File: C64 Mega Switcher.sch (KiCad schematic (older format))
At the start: 11 parts, among them J1 Port 2, J2 Port 1, J3 sega_joypad

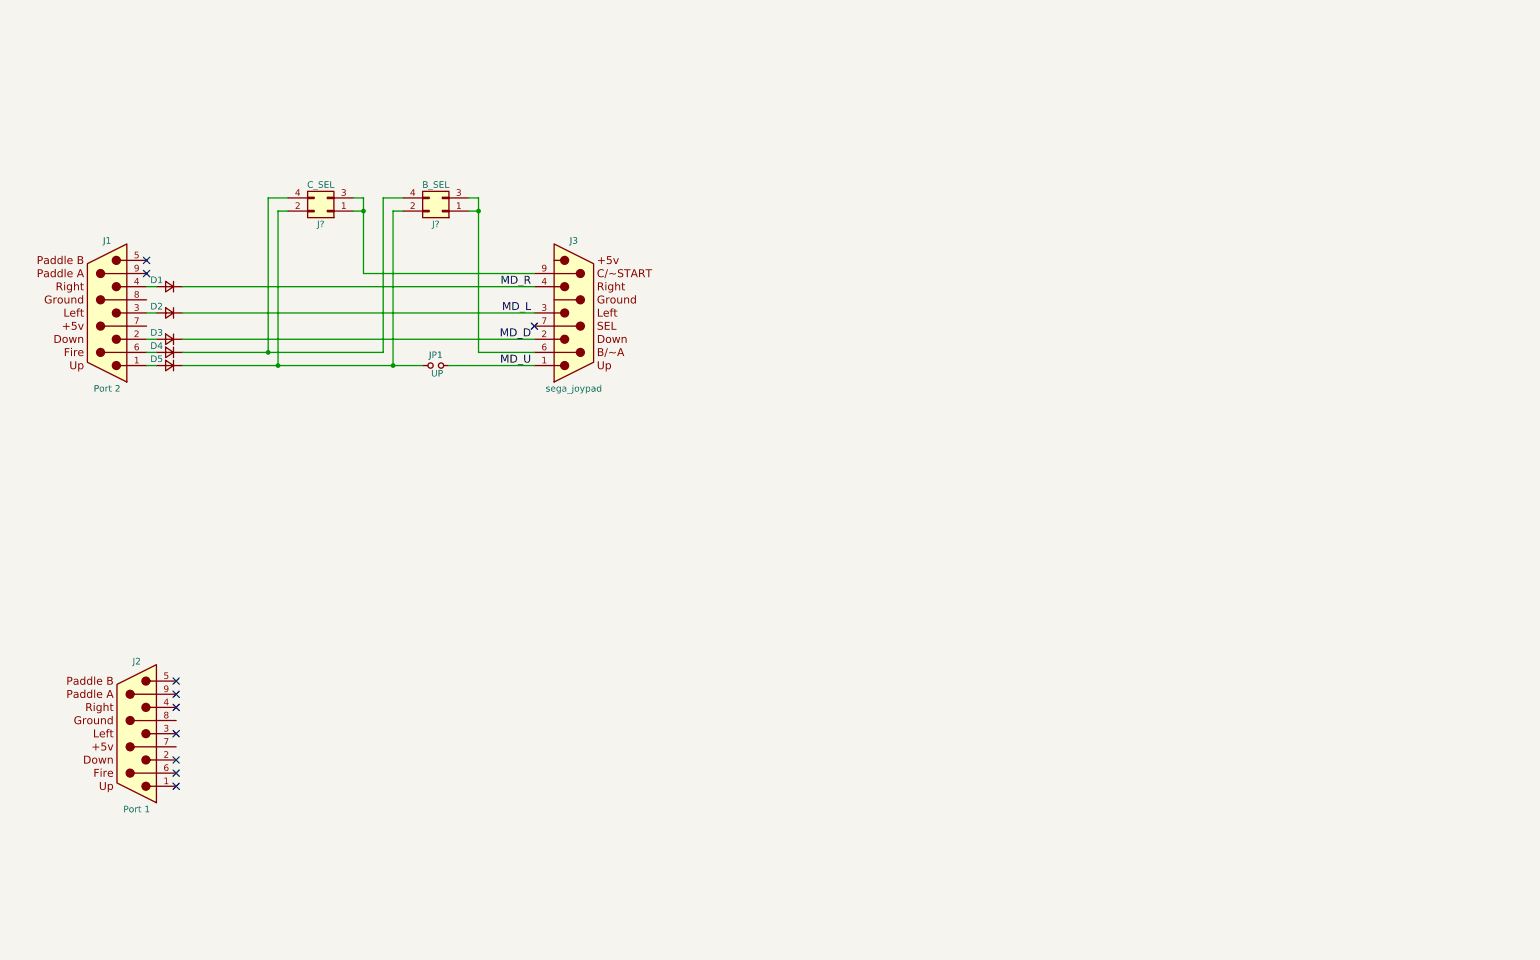
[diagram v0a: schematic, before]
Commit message: Added joystick switcher and assigned footprints.
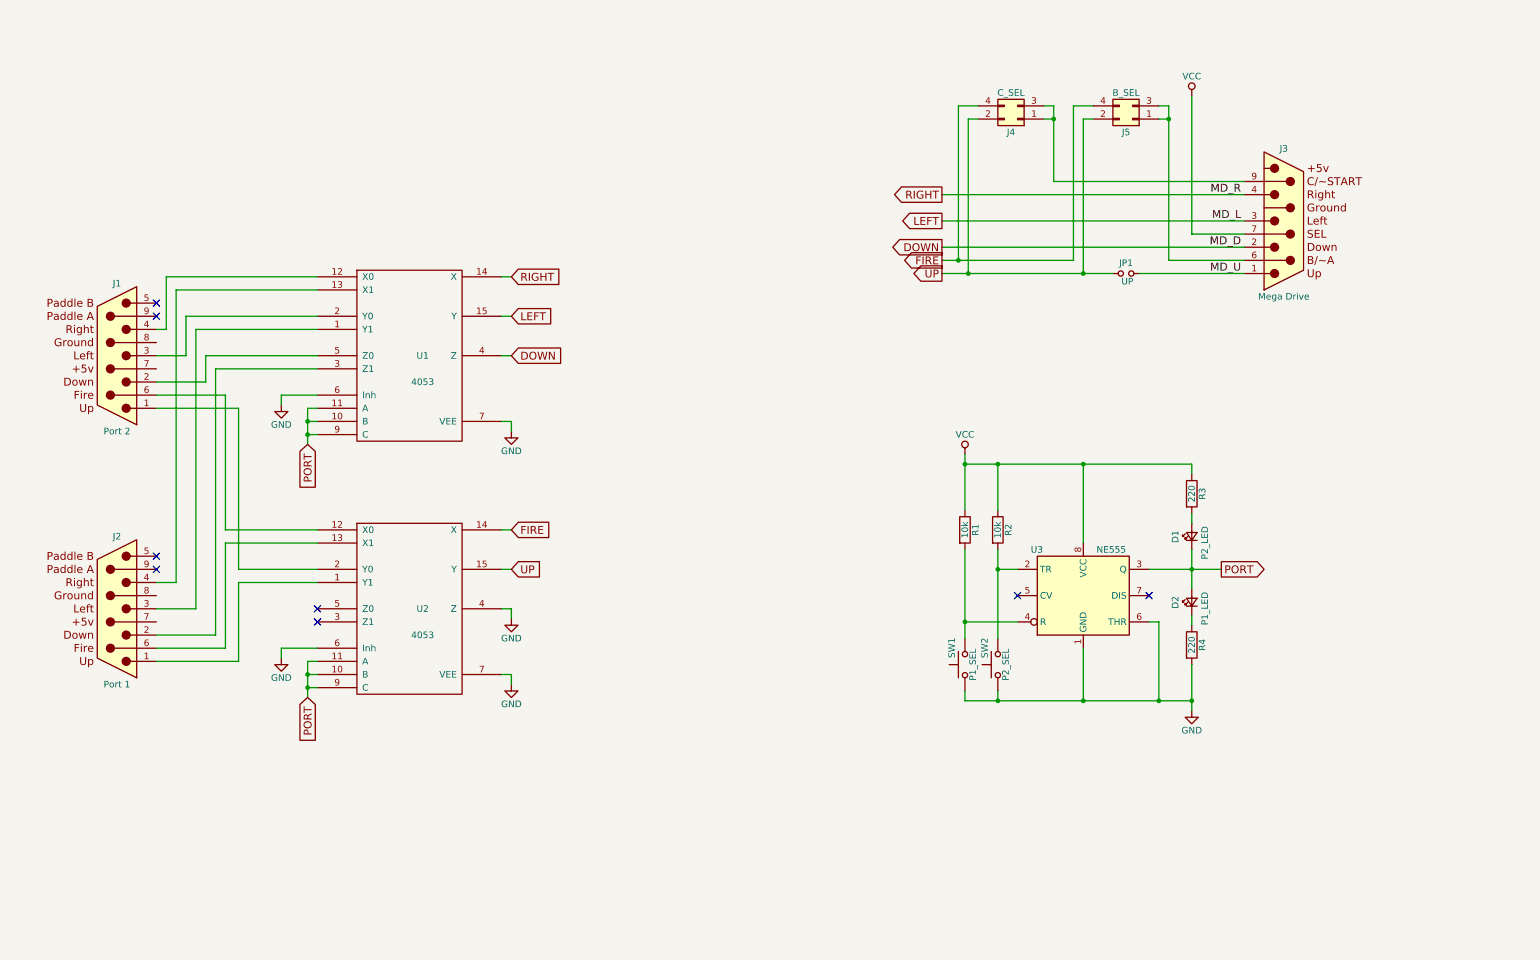
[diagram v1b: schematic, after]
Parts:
- removed D1, D2, D3, D4, D5: 1N4148, Diodes_THT:D_DO-35_SOD27_P7.62mm_Horizontal, symbol D_Small
- added D1: P2_LED, LEDs:LED_D5.0mm, symbol LED_Small
- added D2: P1_LED, LEDs:LED_D5.0mm, symbol LED_Small
- added R1, R2: 10k, Resistors_THT:R_Axial_DIN0207_L6.3mm_D2.5mm_P10.16mm_Horizontal, symbol R
- added R3, R4: 220, Resistors_THT:R_Axial_DIN0207_L6.3mm_D2.5mm_P10.16mm_Horizontal, symbol R
- added SW1: P1_SEL, Buttons_Switches_THT:SW_PUSH_6mm, symbol SW_Push
- added SW2: P2_SEL, Buttons_Switches_THT:SW_PUSH_6mm, symbol SW_Push
- added U1, U2: 4053, Housings_DIP:DIP-16_W7.62mm_Socket, symbol 4053
- added U3: NE555, Housings_DIP:DIP-8_W7.62mm_Socket, symbol NE555
- J1, J2: footprint RND:DSUB-9_Male_Vertical_Pitch2.77x2.84mm -> RND:DSUB-9_Female_Horizontal_P2.77x2.84mm_EdgePinOffset7.70mm_Housed_MountingHolesOffset9.12mm
- J3: value sega_joypad -> Mega Drive; footprint RND:DSUB-9_Male_Vertical_Pitch2.77x2.84mm -> RND:DSUB-9_Male_Horizontal_P2.77x2.84mm_EdgePinOffset7.70mm_Housed_MountingHolesOffset9.12mm
- J4, J5: renamed from J?; footprint (none) -> Pin_Headers:Pin_Header_Straight_2x02_Pitch2.54mm
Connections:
- net GND: now also R4.2, SW1.1, SW2.1, U1.6 (Inh), U1.7 (VEE), U2.4 (Z), U2.6 (Inh), U2.7 (VEE), U3.1 (GND), U3.6 (THR)
- net VCC: now also J3.7, R1.1, R2.1, R3.1, U3.8 (VCC)
- net at J1.1: now also U2.2 (Y0)
- net at J1.2: now also U1.5 (Z0)
- net at J1.3: now also U1.2 (Y0)
- net at J1.4: now also U1.12 (X0)
- net at J1.6: now also U2.12 (X0)
- net at J2.1: now also U2.1 (Y1)
- net at J2.2: now also U1.3 (Z1)
- net at J2.3: now also U1.1 (Y1)
- net at J2.4: now also U1.13 (X1)
- net at J2.6: now also U2.13 (X1)
- net FIRE: now reaches J4.4 (Pin_4), J5.4 (Pin_4)
- net FIRE: now also U2.14 (X)
- net UP: now reaches J4.2 (Pin_2), J5.2 (Pin_2), JP1.1
- net UP: now also U2.15 (Y)
- net MD_D renamed DOWN
- net DOWN: now also U1.4 (Z)
- net MD_L renamed LEFT
- net LEFT: now also U1.15 (Y)
- net MD_R renamed RIGHT
- net RIGHT: now also U1.14 (X)
- new net: R2.2, SW2.2, U3.2 (TR)
- new net: R1.2, SW1.2, U3.4 (R)
- new net: D2.1 (K), R4.1
- new net: D1.2 (A), R3.2
- new net PORT: D1.1 (K), D2.2 (A), U1.10 (B), U1.11 (A), U1.9 (C), U2.10 (B), U2.11 (A), U2.9 (C), U3.3 (Q)
- new net VDD: U1.16 (VDD), U2.16 (VDD)
- new net VSS: U1.8 (VSS), U2.8 (VSS)
- no-connect marks 10 -> 8
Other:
- moved on the sheet: J1, J2, J3, J4, J5, JP1

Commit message: Fixed schematic validations
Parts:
- removed U1, U2: 4053, Housings_DIP:DIP-16_W7.62mm_Socket, symbol 4053
- added C1, C2, C3: 100nF, Capacitors_THT:C_Disc_D4.7mm_W2.5mm_P5.00mm, symbol C_Small
- added U1, U2: 74HCT4053, symbol 74HCT4053
- J1: renamed from J2; symbol Atari_Joystick -> Atari_Joystick_Passive
- renumbered J1 to J2
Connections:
- net DOWN: now also U1.4 (Z)
- net FIRE: now also U2.14 (X)
- net GND: now also J1.8 (GND), J2.8 (GND), C1.2, C2.2, C3.2, U1.6 (Inh), U1.7 (VEE), U1.8 (GND), U2.4 (Z), U2.6 (Inh), U2.7 (VEE), U2.8 (GND)
- net LEFT: now also U1.15 (Y)
- net PORT: now also U1.10 (B), U1.11 (A), U1.9 (C), U2.10 (B), U2.11 (A), U2.9 (C)
- net RIGHT: now also U1.14 (X)
- net UP: now also U2.15 (Y)
- net VCC: now also J1.7 (VCC), J2.7 (VCC), C1.1, C2.1, C3.1, U1.16 (VCC), U2.16 (VCC)
- net at J2.1: now also U2.2 (Y0)
- net at J2.2: now also U1.5 (Z0)
- net at J2.3: now also U1.2 (Y0)
- net at J2.4: now also U1.12 (X0)
- net at J2.6: now also U2.12 (X0)
- net at J1.1: now also U2.1 (Y1)
- net at J1.2: now also U1.3 (Z1)
- net at J1.3: now also U1.1 (Y1)
- net at J1.4: now also U1.13 (X1)
- net at J1.6: now also U2.13 (X1)
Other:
- moved on the sheet: J1, J2

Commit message: General part placement
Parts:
- U1, U2: footprint (none) -> Housings_DIP:DIP-16_W7.62mm_Socket
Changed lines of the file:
@@
 F 0 "U1" H 3550 3150 50  0000 C CNN
 F 1 "74HCT4053" H 3550 2950 50  0000 C CNN
-F 2 "" H 3550 3150 60  0001 C CNN
+F 2 "Housings_DIP:DIP-16_W7.62mm_Socket" H 3550 3150 60  0001 C CNN
 F 3 "" H 3550 3150 60  0001 C CNN
 	1    3550 3150
@@
 F 0 "U2" H 3550 5075 50  0000 C CNN
 F 1 "74HCT4053" H 3550 4875 50  0000 C CNN
-F 2 "" H 3550 5075 60  0001 C CNN
+F 2 "Housings_DIP:DIP-16_W7.62mm_Socket" H 3550 5075 60  0001 C CNN
 F 3 "" H 3550 5075 60  0001 C CNN
 	1    3550 5075

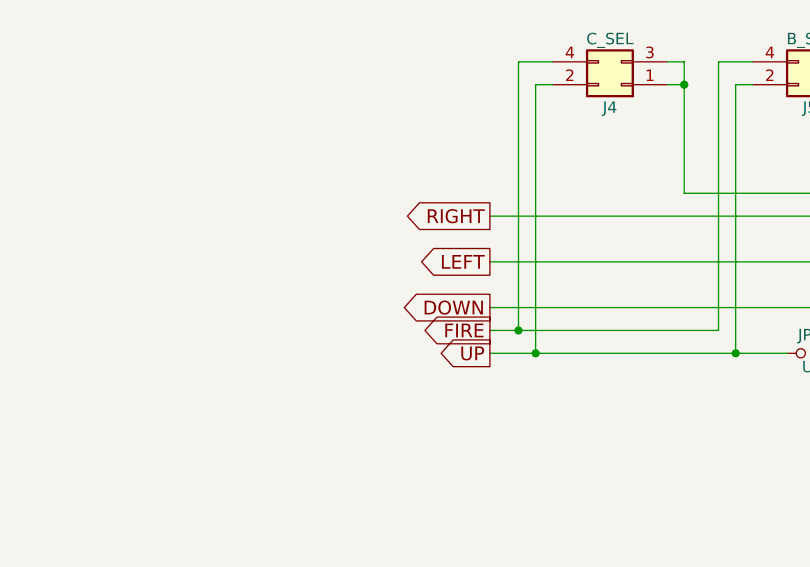
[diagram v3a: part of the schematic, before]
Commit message: Added protection diodes
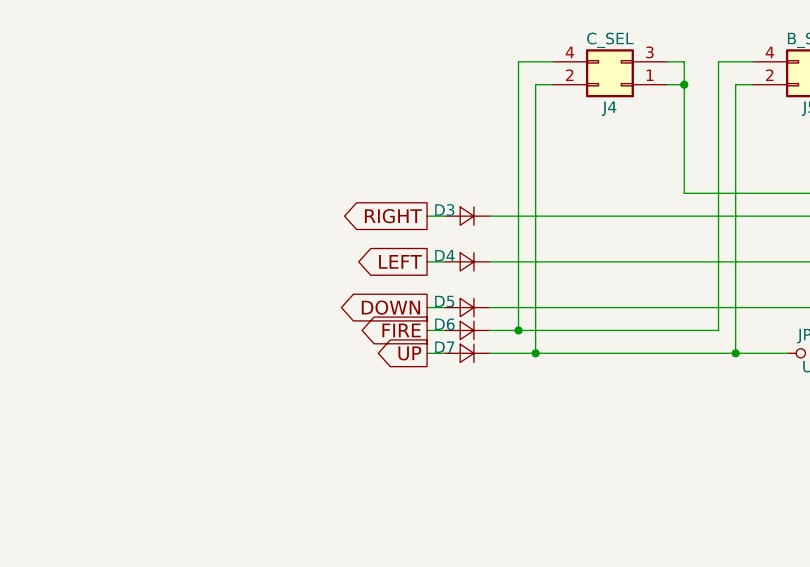
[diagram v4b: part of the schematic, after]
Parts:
- added D3, D4, D5, D6, D7: 1N4148, Diodes_THT:D_DO-35_SOD27_P2.54mm_Vertical_AnodeUp, symbol D_Small
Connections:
- net DOWN: now also D5.2 (A); no longer J3.2
- net FIRE: now also D6.2 (A); no longer J4.4 (Pin_4), J5.4 (Pin_4)
- net LEFT: now also D4.2 (A); no longer J3.3
- net RIGHT: now also D3.2 (A); no longer J3.4
- net UP: now also D7.2 (A); no longer J4.2 (Pin_2), J5.2 (Pin_2), JP1.1
- new net: D7.1 (K), J4.2 (Pin_2), J5.2 (Pin_2), JP1.1
- new net: D6.1 (K), J4.4 (Pin_4), J5.4 (Pin_4)
- new net MD_D: D5.1 (K), J3.2
- new net MD_L: D4.1 (K), J3.3
- new net MD_R: D3.1 (K), J3.4
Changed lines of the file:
@@
 Text GLabel 4325 2550 2    60   Input ~ 0
 RIGHT
-Text GLabel 7600 2125 0    60   Output ~ 0
+Text GLabel 7325 2125 0    60   Output ~ 0
 LEFT
-Text GLabel 7600 2325 0    60   Output ~ 0
+Text GLabel 7325 2325 0    60   Output ~ 0
 DOWN
-Text GLabel 7600 2525 0    60   Output ~ 0
+Text GLabel 7325 2525 0    60   Output ~ 0
 UP
-Text GLabel 7600 2425 0    60   Output ~ 0
+Text GLabel 7325 2425 0    60   Output ~ 0
 FIRE
 NoConn ~ 1475 2750
@@
 Text GLabel 4325 2850 2    60   Input ~ 0
 LEFT
-Text GLabel 7600 1925 0    60   Output ~ 0
+Text GLabel 7325 1925 0    60   Output ~ 0
 RIGHT
 Text GLabel 4325 3150 2    60   Input ~ 0
@@
 	0    -1   -1   0
 $EndComp
+$Comp
+L D_Small D3
+U 1 1 5D13AE84
+P 7500 1925
+F 0 "D3" H 7550 1900 50  0000 L CNN
+F 1 "1N4148" H 7350 1845 50  0001 L CNN
+F 2 "Diodes_THT:D_DO-35_SOD27_P2.54mm_Vertical_AnodeUp" V 7500 1925 50  0001 C CNN
+F 3 "" V 7500 1925 50  0001 C CNN
+	1    7500 1925
+	-1   0    0    1
+$EndComp
+Wire Wire Line
+	7400 1925 7325 1925
+$Comp
+L D_Small D4
+U 1 1 5D13B3D4
+P 7500 2125
+F 0 "D4" H 7550 2100 50  0000 L CNN
+F 1 "1N4148" H 7350 2045 50  0001 L CNN
+F 2 "Diodes_THT:D_DO-35_SOD27_P2.54mm_Vertical_AnodeUp" V 7500 2125 50  0001 C CNN
+F 3 "" V 7500 2125 50  0001 C CNN
+	1    7500 2125
+	-1   0    0    1
+$EndComp
+Wire Wire Line
+	7400 2125 7325 2125
+$Comp
+L D_Small D5
+U 1 1 5D13B416
+P 7500 2325
+F 0 "D5" H 7550 2300 50  0000 L CNN
+F 1 "1N4148" H 7350 2245 50  0001 L CNN
+F 2 "Diodes_THT:D_DO-35_SOD27_P2.54mm_Vertical_AnodeUp" V 7500 2325 50  0001 C CNN
+F 3 "" V 7500 2325 50  0001 C CNN
+	1    7500 2325
+	-1   0    0    1
+$EndComp
+Wire Wire Line
+	7400 2325 7325 2325
+$Comp
+L D_Small D6
+U 1 1 5D13B464
+P 7500 2425
+F 0 "D6" H 7550 2400 50  0000 L CNN
+F 1 "1N4148" H 7350 2345 50  0001 L CNN
+F 2 "Diodes_THT:D_DO-35_SOD27_P2.54mm_Vertical_AnodeUp" V 7500 2425 50  0001 C CNN
+F 3 "" V 7500 2425 50  0001 C CNN
+	1    7500 2425
+	-1   0    0    1
+$EndComp
+Wire Wire Line
+	7400 2425 7325 2425
+$Comp
+L D_Small D7
+U 1 1 5D13B4A8
+P 7500 2525
+F 0 "D7" H 7550 2500 50  0000 L CNN
+F 1 "1N4148" H 7350 2445 50  0001 L CNN
+F 2 "Diodes_THT:D_DO-35_SOD27_P2.54mm_Vertical_AnodeUp" V 7500 2525 50  0001 C CNN
+F 3 "" V 7500 2525 50  0001 C CNN
+	1    7500 2525
+	-1   0    0    1
+$EndComp
+Wire Wire Line
+	7400 2525 7325 2525
 $EndSCHEMATC
